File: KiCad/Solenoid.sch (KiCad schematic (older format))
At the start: 4 parts

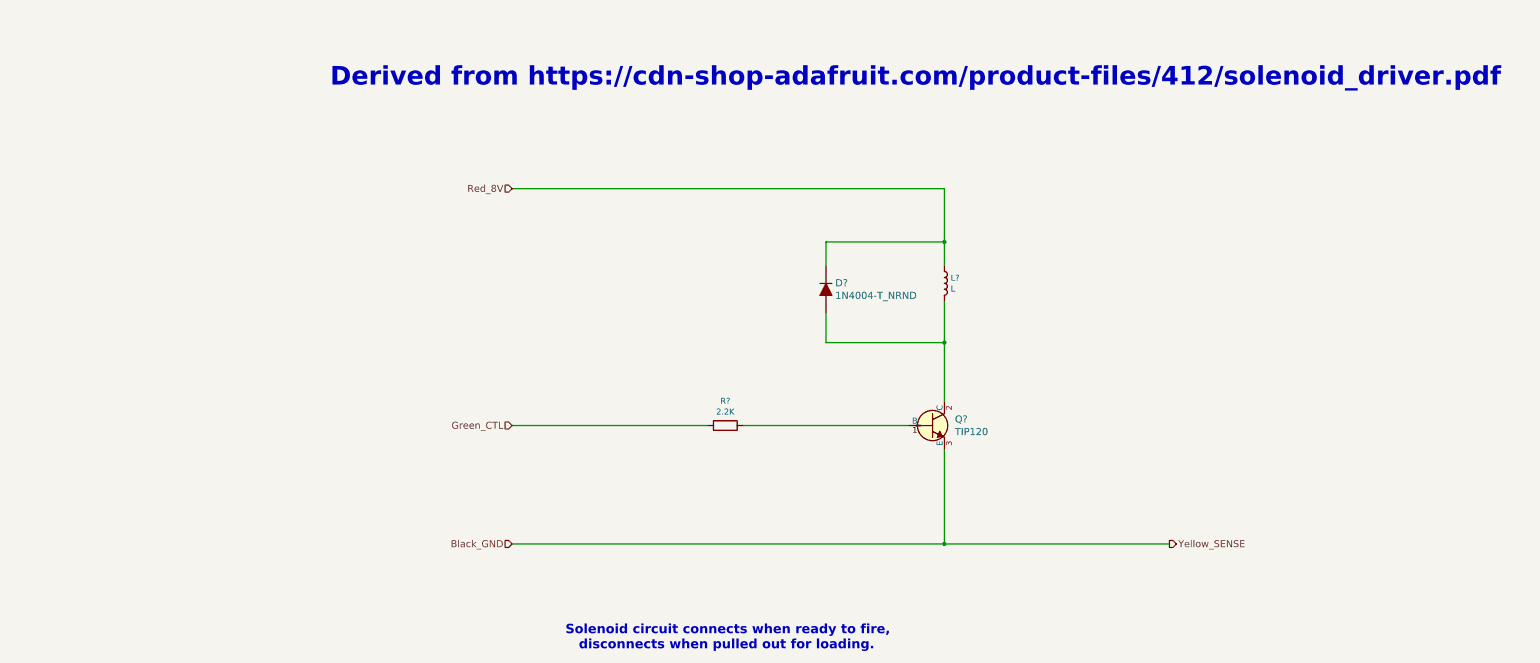
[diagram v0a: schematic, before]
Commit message: update schematic solenoid circuit
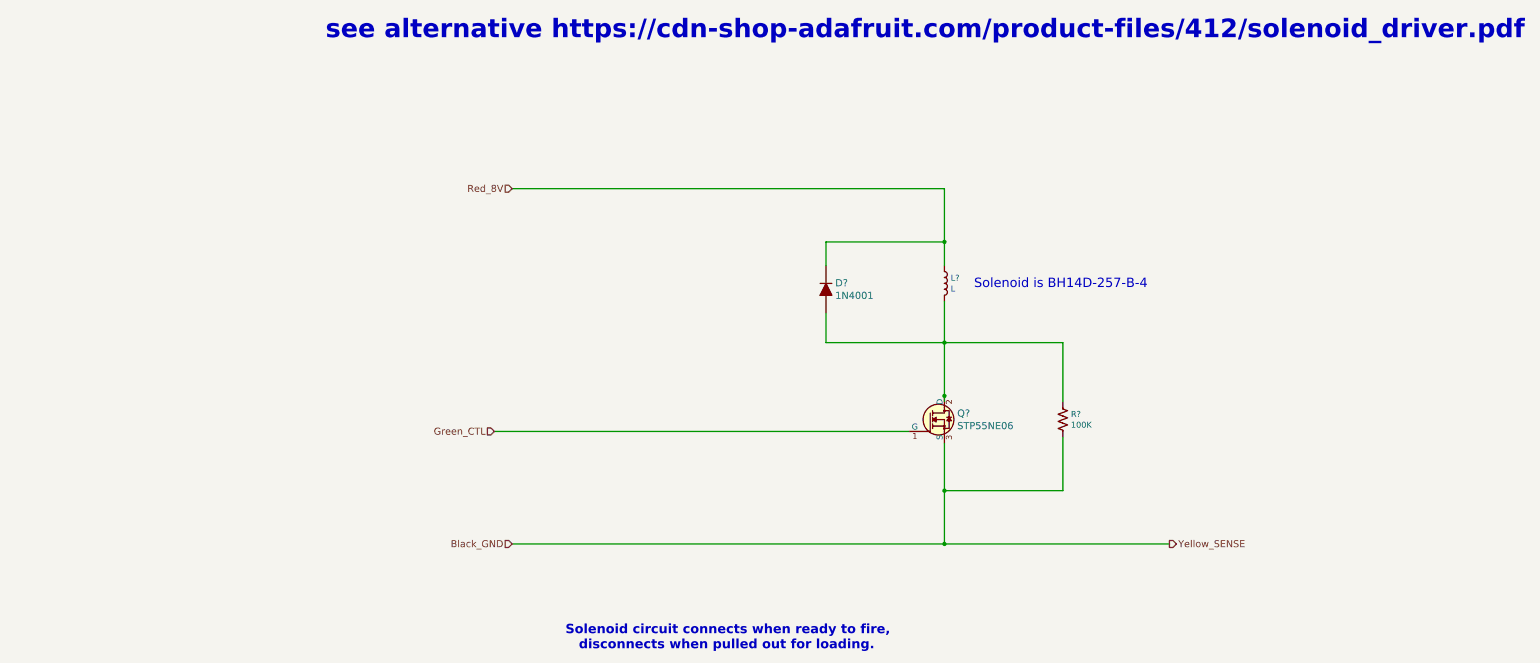
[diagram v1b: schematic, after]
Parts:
- removed Q?: TIP120, digikey-footprints:TO-220-3, symbol dk_Transistors-Bipolar-BJT-Single:TIP120
- removed R?: 2.2K, symbol Device:R
- added Q?: STP55NE06, digikey-footprints:TO-220-3, symbol dk_Transistors-FETs-MOSFETs-Single:FQP30N06L
- added R?: 100K, symbol Device:R_US
- D?: value 1N4004-T_NRND -> 1N4001
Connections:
- wire segments 14 -> 19
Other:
- note added: "Solenoid is BH14D-257-B-4"
- note added: "see alternative https://cdn-shop-adafruit.com/product-files/412/solenoid_driver.pdf"
- note removed: "Derived from https://cdn-shop-adafruit.com/product-files/412/solenoid_driver.pdf"
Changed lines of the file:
@@
 Sheet 2 4
 Title "Detail: Solenoid Driver"
-Date "2021-09-05"
+Date "2021-10-05"
 Rev ""
 Comp ""
@@
 P 5150 3350
 F 0 "D?" V 5203 3272 60  0000 R CNN
-F 1 "1N4004-T_NRND" V 5097 3272 60  0000 R CNN
+F 1 "1N4001" V 5097 3272 60  0000 R CNN
 F 2 "digikey-footprints:DO-41" H 5350 3550 60  0001 L CNN
 F 3 "https://www.diodes.com/assets/Datasheets/ds28002.pdf" H 5350 3650 60  0001 L CNN
@@
 	1    0    0    -1
 $EndComp
-$Comp
-L dk_Transistors-Bipolar-BJT-Single:TIP120 Q?
-U 1 1 5F12FE09
-P 6050 4500
-F 0 "Q?" H 6238 4553 60  0000 L CNN
-F 1 "TIP120" H 6238 4447 60  0000 L CNN
-F 2 "digikey-footprints:TO-220-3" H 6250 4700 60  0001 L CNN
-F 3 "http://www.st.com/content/ccc/resource/technical/document/datasheet/f9/ed/f5/44/26/b9/43/a4/CD00000911.pdf/files/CD00000911.pdf/jcr:content/translations/en.CD00000911.pdf" H 6250 4800 60  0001 L CNN
-F 4 "497-2539-5-ND" H 6250 4900 60  0001 L CNN "Digi-Key_PN"
-F 5 "TIP120" H 6250 5000 60  0001 L CNN "MPN"
-F 6 "Discrete Semiconductor Products" H 6250 5100 60  0001 L CNN "Category"
-F 7 "Transistors - Bipolar (BJT) - Single" H 6250 5200 60  0001 L CNN "Family"
-F 8 "http://www.st.com/content/ccc/resource/technical/document/datasheet/f9/ed/f5/44/26/b9/43/a4/CD00000911.pdf/files/CD00000911.pdf/jcr:content/translations/en.CD00000911.pdf" H 6250 5300 60  0001 L CNN "DK_Datasheet_Link"
-F 9 "/product-detail/en/stmicroelectronics/TIP120/497-2539-5-ND/603564" H 6250 5400 60  0001 L CNN "DK_Detail_Page"
-F 10 "TRANS NPN DARL 60V 5A TO-220" H 6250 5500 60  0001 L CNN "Description"
-F 11 "STMicroelectronics" H 6250 5600 60  0001 L CNN "Manufacturer"
-F 12 "Active" H 6250 5700 60  0001 L CNN "Status"
-	1    6050 4500
-	1    0    0    -1
-$EndComp
-$Comp
-L Device:R R?
-U 1 1 5F130714
-P 4300 4500
-F 0 "R?" V 4093 4500 50  0000 C CNN
-F 1 "2.2K" V 4184 4500 50  0000 C CNN
-F 2 "" V 4230 4500 50  0001 C CNN
-F 3 "~" H 4300 4500 50  0001 C CNN
-	1    4300 4500
-	0    1    1    0
-$EndComp
 Wire Wire Line
 	6150 2500 6150 2950
@@
 	6150 3450 6150 3800
 Wire Wire Line
-	5850 4500 4450 4500
-Wire Wire Line
 	5150 3550 5150 3800
 Wire Wire Line
 	5150 3800 6150 3800
-Connection ~ 6150 3800
-Wire Wire Line
-	6150 3800 6150 4300
 Text HLabel 2500 2500 0    59   Input ~ 0
 Red_8V
-Text HLabel 2500 4500 0    59   Input ~ 0
+Text HLabel 2350 4550 0    59   Input ~ 0
 Green_CTL
 Text HLabel 2500 5500 0    59   Input ~ 0
@@
 Yellow_SENSE
 Wire Wire Line
+	2500 2500 6150 2500
+Text Notes 11050 1250 2    157  ~ 31
+see alternative https://cdn-shop-adafruit.com/product-files/412/solenoid_driver.pdf
+Text Notes 2950 6400 0    79   ~ 16
+Solenoid circuit connects when ready to fire,\n   disconnects when pulled out for loading.
+$Comp
+L dk_Transistors-FETs-MOSFETs-Single:FQP30N06L Q?
+U 1 1 615DBD24
+P 6150 4450
+F 0 "Q?" H 6258 4503 60  0000 L CNN
+F 1 "STP55NE06" H 6258 4397 60  0000 L CNN
+F 2 "digikey-footprints:TO-220-3" H 6350 4650 60  0001 L CNN
+F 3 "https://www.onsemi.com/pub/Collateral/FQP30N06L-D.pdf" H 6350 4750 60  0001 L CNN
+F 4 "FQP30N06L-ND" H 6350 4850 60  0001 L CNN "Digi-Key_PN"
+F 5 "FQP30N06L" H 6350 4950 60  0001 L CNN "MPN"
+F 6 "Discrete Semiconductor Products" H 6350 5050 60  0001 L CNN "Category"
+F 7 "Transistors - FETs, MOSFETs - Single" H 6350 5150 60  0001 L CNN "Family"
+F 8 "https://www.onsemi.com/pub/Collateral/FQP30N06L-D.pdf" H 6350 5250 60  0001 L CNN "DK_Datasheet_Link"
+F 9 "/product-detail/en/on-semiconductor/FQP30N06L/FQP30N06L-ND/1055122" H 6350 5350 60  0001 L CNN "DK_Detail_Page"
+F 10 "MOSFET N-CH 60V 32A TO-220" H 6350 5450 60  0001 L CNN "Description"
+F 11 "ON Semiconductor" H 6350 5550 60  0001 L CNN "Manufacturer"
+F 12 "Active" H 6350 5650 60  0001 L CNN "Status"
+	1    6150 4450
+	1    0    0    -1
+$EndComp
+Wire Wire Line
 	2500 5500 6150 5500
 Wire Wire Line
-	6150 5500 6150 4700
+	6150 3800 6150 4250
+Connection ~ 6150 3800
+Connection ~ 6150 4250
 Wire Wire Line
-	8050 5500 6150 5500
+	6150 4250 6150 4300
+Wire Wire Line
+	6150 4650 6150 5050
 Connection ~ 6150 5500
 Wire Wire Line
-	2500 4500 4150 4500
+	6150 5500 8050 5500
+$Comp
+L Device:R_US R?
+U 1 1 615DF9FD
+P 7150 4450
+F 0 "R?" H 7218 4496 50  0000 L CNN
+F 1 "100K" H 7218 4405 50  0000 L CNN
+F 2 "" V 7190 4440 50  0001 C CNN
+F 3 "~" H 7150 4450 50  0001 C CNN
+	1    7150 4450
+	1    0    0    -1
+$EndComp
 Wire Wire Line
-	2500 2500 6150 2500
-Text Notes 10850 1650 2    157  ~ 31
-Derived from https://cdn-shop-adafruit.com/product-files/412/solenoid_driver.pdf
-Text Notes 2950 6400 0    79   ~ 16
-Solenoid circuit connects when ready to fire,\n   disconnects when pulled out for loading.
+	6150 3800 7150 3800
+Wire Wire Line
+	7150 3800 7150 4300
+Wire Wire Line
+	7150 4600 7150 5050
+Wire Wire Line
+	7150 5050 6150 5050
+Connection ~ 6150 5050
+Wire Wire Line
+	6150 5050 6150 5500
+Text Notes 6400 3350 0    79   ~ 0
+Solenoid is BH14D-257-B-4
+Wire Wire Line
+	5850 4550 2350 4550
 $EndSCHEMATC

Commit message: add motor circuit for SIDEWINDER on sheet for solenoid for SILVER
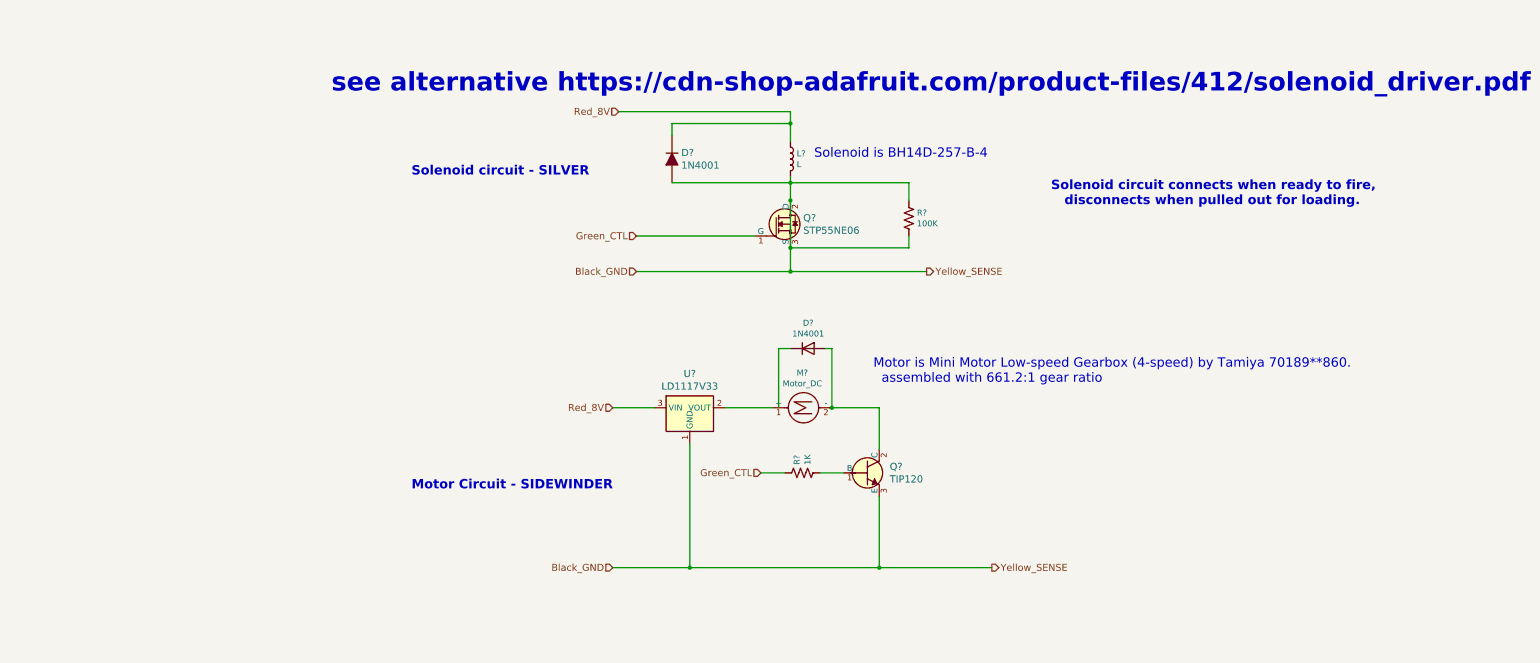
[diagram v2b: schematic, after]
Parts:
- added D?: 1N4001, Diode_THT:D_DO-41_SOD81_P10.16mm_Horizontal, symbol Diode:1N4001
- added M?: Motor_DC, symbol Motor:Motor_DC
- added Q?: TIP120, digikey-footprints:TO-220-3, symbol dk_Transistors-Bipolar-BJT-Single:TIP120
- added R?: 1K, symbol Device:R_US
- added U?: LD1117V33, digikey-footprints:TO-220-3, symbol dk_PMIC-Voltage-Regulators-Linear:LD1117V33
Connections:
- wire segments 19 -> 32
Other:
- note added: "Motor Circuit - SIDEWINDER"
- note added: "Motor is Mini Motor Low-speed Gearbox (4-speed) by Tamiya 70189**860.\n assembled with 661.2:1 gear ratio"
- note added: "Solenoid circuit - SILVER"
- moved on the sheet: D?, L?, Q?, R?
